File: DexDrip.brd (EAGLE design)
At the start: 53 x 30 mm, 57 parts, among them CN2 M02JST-PTH-2, IC7 TLV71333DBV, U1 MCP73831, X1 Micro USB, Y1 48mHz Abracon

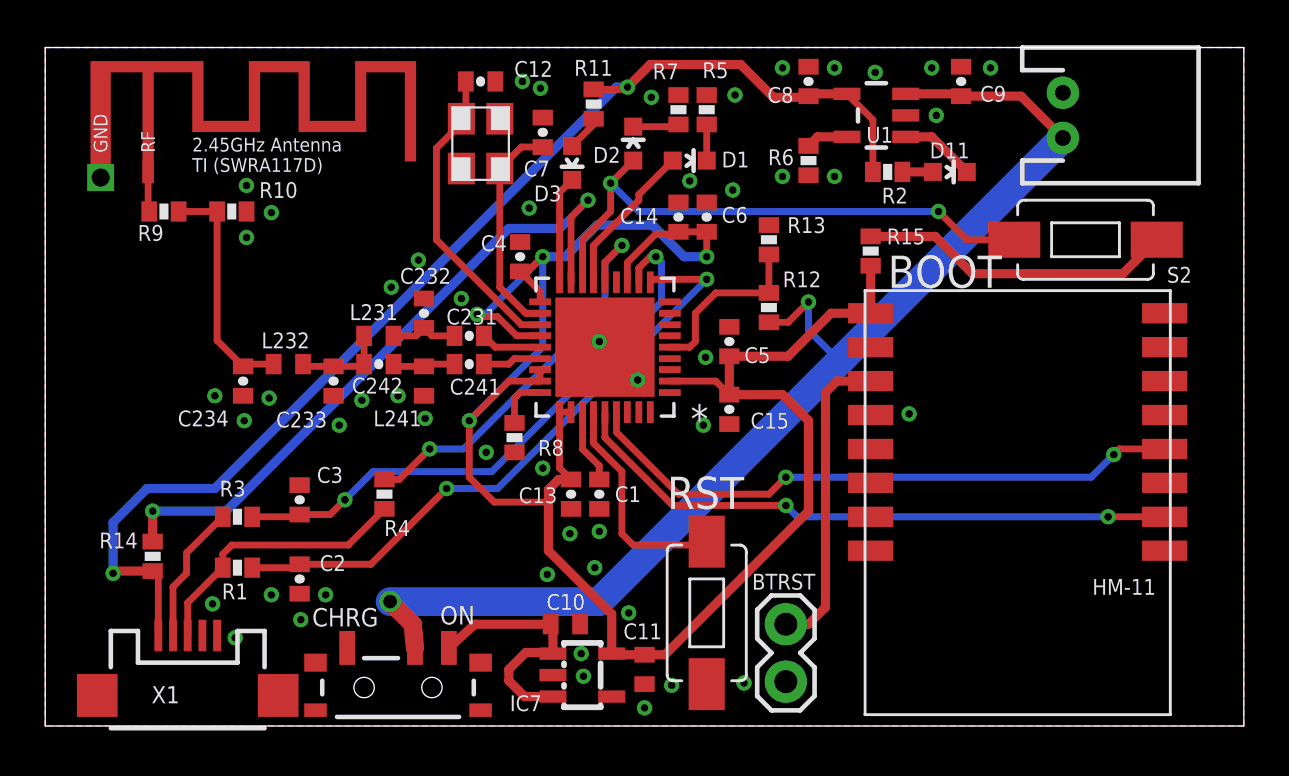
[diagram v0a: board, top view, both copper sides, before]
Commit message: Added programming pins
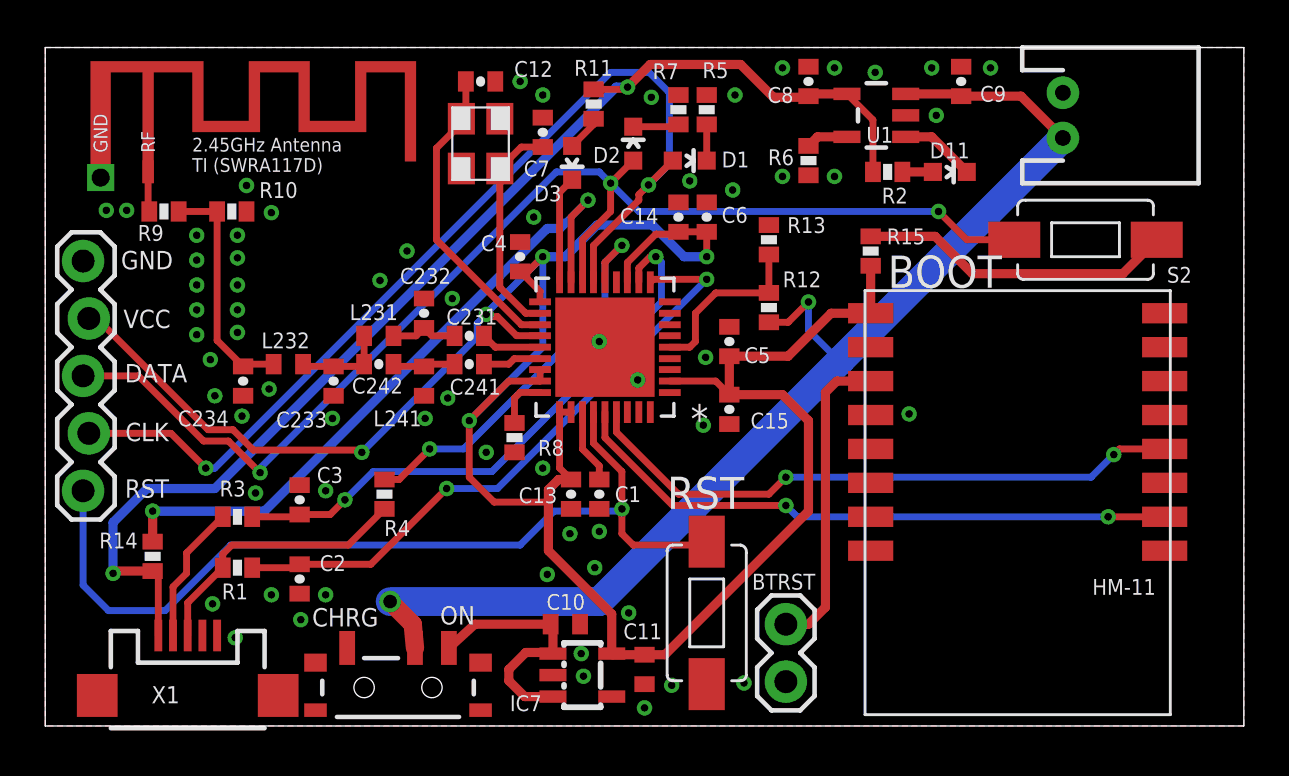
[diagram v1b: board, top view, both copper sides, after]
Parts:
- added JP1: (no value), SparkFun-Connectors:1X05_LOCK
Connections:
- removed net BOOT: D2.A, S2.P$2, U$11.16
- removed net N$11: D1.A, U$11.15
- new net DBG_CLK: D2.A, JP1.3, S2.P$2, U$11.16
- new net DBG_DATA: D1.A, JP1.2, U$11.15
- net GND: now also JP1.5
- net VCC: now also JP1.4
- net WRST: now also JP1.1
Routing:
- net DBG_CLK: track 0.00 -> 56.1 mm, vias 0 -> 3
- net DBG_DATA: track 0.00 -> 45.2 mm, vias 0 -> 2
- net WRST: track 9.92 -> 40.3 mm, vias 0 -> 1
- net BOOT: track 25.2 -> 0.00 mm, vias 2 -> 0
- net VCC: track 90.3 -> 112.5 mm, vias 4 -> 5
- net N$11: track 6.83 -> 0.00 mm
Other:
- board text added: "CLK"
- board text added: "DATA"
- board text added: "GND"
- board text added: "VCC"

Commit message: Added BOM
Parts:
- moved JP1 0.60 mm to (1.40, 10.4)
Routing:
- net DBG_DATA: track 45.2 -> 44.6 mm
- net DBG_CLK: track 56.1 -> 55.5 mm
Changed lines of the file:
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@@
 <element name="LOGO1" library="IdleHandsProject" package="IHD-LOGO-S" value="IDLEHANDS_LOGOS" x="43.7" y="13.1" rot="MR180"/>
 <element name="LOGO2" library="SparkFun-Aesthetics" package="OSHW-LOGO-S" value="OSHW-LOGOS" x="39.7" y="13" rot="MR0"/>
-<element name="JP1" library="SparkFun-Connectors" package="1X05_LOCK" value="" x="0.8" y="10.4" smashed="yes" rot="R90">
-<attribute name="VALUE" x="3.975" y="9.13" size="1.27" layer="27" rot="R90"/>
+<element name="JP1" library="SparkFun-Connectors" package="1X05_LOCK" value="" x="1.4" y="10.4" smashed="yes" rot="R90">
+<attribute name="VALUE" x="4.575" y="9.13" size="1.27" layer="27" rot="R90"/>
 </element>
 </elements>
@@
 <wire x1="18.1" y1="17.2" x2="13" y2="12.1" width="0.3048" layer="16"/>
 <via x="13" y="12.1" extent="1-16" drill="0.3302"/>
-<wire x1="0.947" y1="18" x2="0.927" y2="18.02" width="0.3048" layer="1"/>
 <wire x1="8.2" y1="12.2" x2="12.9" y2="12.2" width="0.3048" layer="1"/>
 <wire x1="12.9" y1="12.2" x2="13" y2="12.1" width="0.3048" layer="1"/>
-<wire x1="0.947" y1="18" x2="1.3" y2="18" width="0.3048" layer="1"/>
-<wire x1="1.3" y1="18" x2="6.2" y2="13.1" width="0.3048" layer="1"/>
 <wire x1="6.2" y1="13.1" x2="7.3" y2="13.1" width="0.3048" layer="1"/>
 <wire x1="7.3" y1="13.1" x2="8.2" y2="12.2" width="0.3048" layer="1"/>
@@
 <wire x1="19" y1="18.1" x2="18.6" y2="18.1" width="0.3048" layer="1"/>
 <wire x1="18.6" y1="18.1" x2="18.5" y2="18.2" width="0.3048" layer="1"/>
+<wire x1="6.2" y1="13.1" x2="1.527" y2="17.773" width="0.3048" layer="1"/>
+<wire x1="1.527" y1="17.773" x2="1.527" y2="18.02" width="0.3048" layer="1"/>
 </signal>
 <signal name="N$6">
@@
 <wire x1="28.1" y1="8" x2="28.25" y2="8.15" width="0.3048" layer="1"/>
 <wire x1="24.5" y1="11.25" x2="24.5" y2="9.6" width="0.3048" layer="1"/>
-<wire x1="24.5" y1="9.3" x2="24.5" y2="8.5" width="0.3048" layer="1"/>
+<wire x1="24.5" y1="9.6" x2="24.5" y2="8.5" width="0.3048" layer="1"/>
 <wire x1="24.5" y1="8.5" x2="25" y2="8" width="0.3048" layer="1"/>
 <contactref element="JP1" pad="1"/>
-<wire x1="0.673" y1="10.4" x2="0.673" y2="6.227" width="0.3048" layer="16"/>
-<wire x1="0.673" y1="6.227" x2="1.8" y2="5.1" width="0.3048" layer="16"/>
 <wire x1="1.8" y1="5.1" x2="4.3" y2="5.1" width="0.3048" layer="16"/>
 <wire x1="4.3" y1="5.1" x2="7.2" y2="8" width="0.3048" layer="16"/>
@@
 <wire x1="24.4" y1="9.5" x2="24.5" y2="9.6" width="0.3048" layer="16"/>
 <via x="24.5" y="9.6" extent="1-16" drill="0.3302"/>
-<wire x1="24.5" y1="9.6" x2="24.5" y2="9.3" width="0.3048" layer="1"/>
+<wire x1="1.8" y1="5.1" x2="0.5" y2="6.4" width="0.3048" layer="16"/>
+<wire x1="0.5" y1="6.4" x2="0.5" y2="9.627" width="0.3048" layer="16"/>
+<wire x1="0.5" y1="9.627" x2="1.273" y2="10.4" width="0.3048" layer="16"/>
 </signal>
 <signal name="N$8">
@@
 <wire x1="25.25" y1="22.75" x2="24" y2="24" width="0.3048" layer="16"/>
 <via x="24" y="24" extent="1-16" drill="0.3302"/>
-<wire x1="0.673" y1="15.48" x2="3.12" y2="15.48" width="0.3048" layer="1"/>
+<wire x1="1.273" y1="15.48" x2="3.12" y2="15.48" width="0.3048" layer="1"/>
 <wire x1="3.12" y1="15.48" x2="6" y2="12.6" width="0.3048" layer="1"/>
 <wire x1="6" y1="12.6" x2="7.1" y2="12.6" width="0.3048" layer="1"/>
@@
 <wire x1="23.242" y1="21.242" x2="25.25" y2="23.25" width="0.3048" layer="1"/>
 <wire x1="25.25" y1="23.25" x2="25.25" y2="23.5" width="0.3048" layer="1"/>
-<wire x1="25.25" y1="23.5" x2="25.475" y2="23.725" width="0.3048" layer="1"/>
+<wire x1="25.25" y1="23.5" x2="25.675" y2="23.925" width="0.3048" layer="1"/>
 <wire x1="25.675" y1="23.925" x2="26.75" y2="25" width="0.3048" layer="1"/>
-<wire x1="0.927" y1="12.94" x2="4.56" y2="12.94" width="0.3048" layer="1"/>
+<wire x1="1.527" y1="12.94" x2="4.56" y2="12.94" width="0.3048" layer="1"/>
 <wire x1="4.56" y1="12.94" x2="6.1" y2="11.4" width="0.3048" layer="1"/>
 <via x="6.1" y="11.4" extent="1-16" drill="0.3302"/>
@@
 <wire x1="26.6" y1="24.85" x2="25.675" y2="23.925" width="0.3048" layer="16"/>
 <via x="25.675" y="23.925" extent="1-16" drill="0.3302"/>
-<wire x1="25.675" y1="23.925" x2="25.475" y2="23.725" width="0.3048" layer="1"/>
 </signal>
 </signals>

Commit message: Fixes some R Values RF WORKING
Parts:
- R10: value 330 -> DNP
- R15: value 330 -> 1k
- R9: value 330 -> 0
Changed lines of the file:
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@@
 <?xml version="1.0" encoding="utf-8"?>
 <!DOCTYPE eagle SYSTEM "eagle.dtd">
-<eagle version="7.1.0">
+<eagle version="7.2.0">
 <drawing>
 <settings>
@@
 <attribute name="NAME" x="8.561" y="16.6985" size="0.7" layer="25" font="vector"/>
 </element>
-<element name="R10" library="SparkFun" package="0402-RES" value="330" x="7.25" y="22.75" smashed="yes">
+<element name="R10" library="SparkFun" package="0402-RES" value="DNP" x="7.25" y="22.75" smashed="yes">
 <attribute name="NAME" x="8.461" y="23.3485" size="0.7" layer="25" font="vector"/>
 </element>
-<element name="R9" library="SparkFun" package="0402-RES" value="330" x="4.25" y="22.75" smashed="yes" rot="R180">
+<element name="R9" library="SparkFun" package="0402-RES" value="0" x="4.25" y="22.75" smashed="yes" rot="R180">
 <attribute name="NAME" x="4.239" y="22.1515" size="0.7" layer="25" font="vector" rot="R180"/>
 </element>
@@
 <attribute name="NAME" x="3.089" y="8.5515" size="0.7" layer="25" font="vector" rot="R180"/>
 </element>
-<element name="R15" library="SparkFun" package="0402-RES" value="330" x="35.5" y="21" smashed="yes" rot="R270">
+<element name="R15" library="SparkFun" package="0402-RES" value="1k" x="35.5" y="21" smashed="yes" rot="R270">
 <attribute name="NAME" x="36.211" y="21.2985" size="0.7" layer="25" font="vector"/>
 </element>
